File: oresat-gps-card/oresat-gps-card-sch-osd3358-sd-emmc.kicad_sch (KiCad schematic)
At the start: 21 parts, among them J4 DM3BT-DSF-PEJS, U1 OSD3358-512M-BSM, U8 TCAN330, U9 EMMC+RESET+5.1-COMPATIBLE-BA

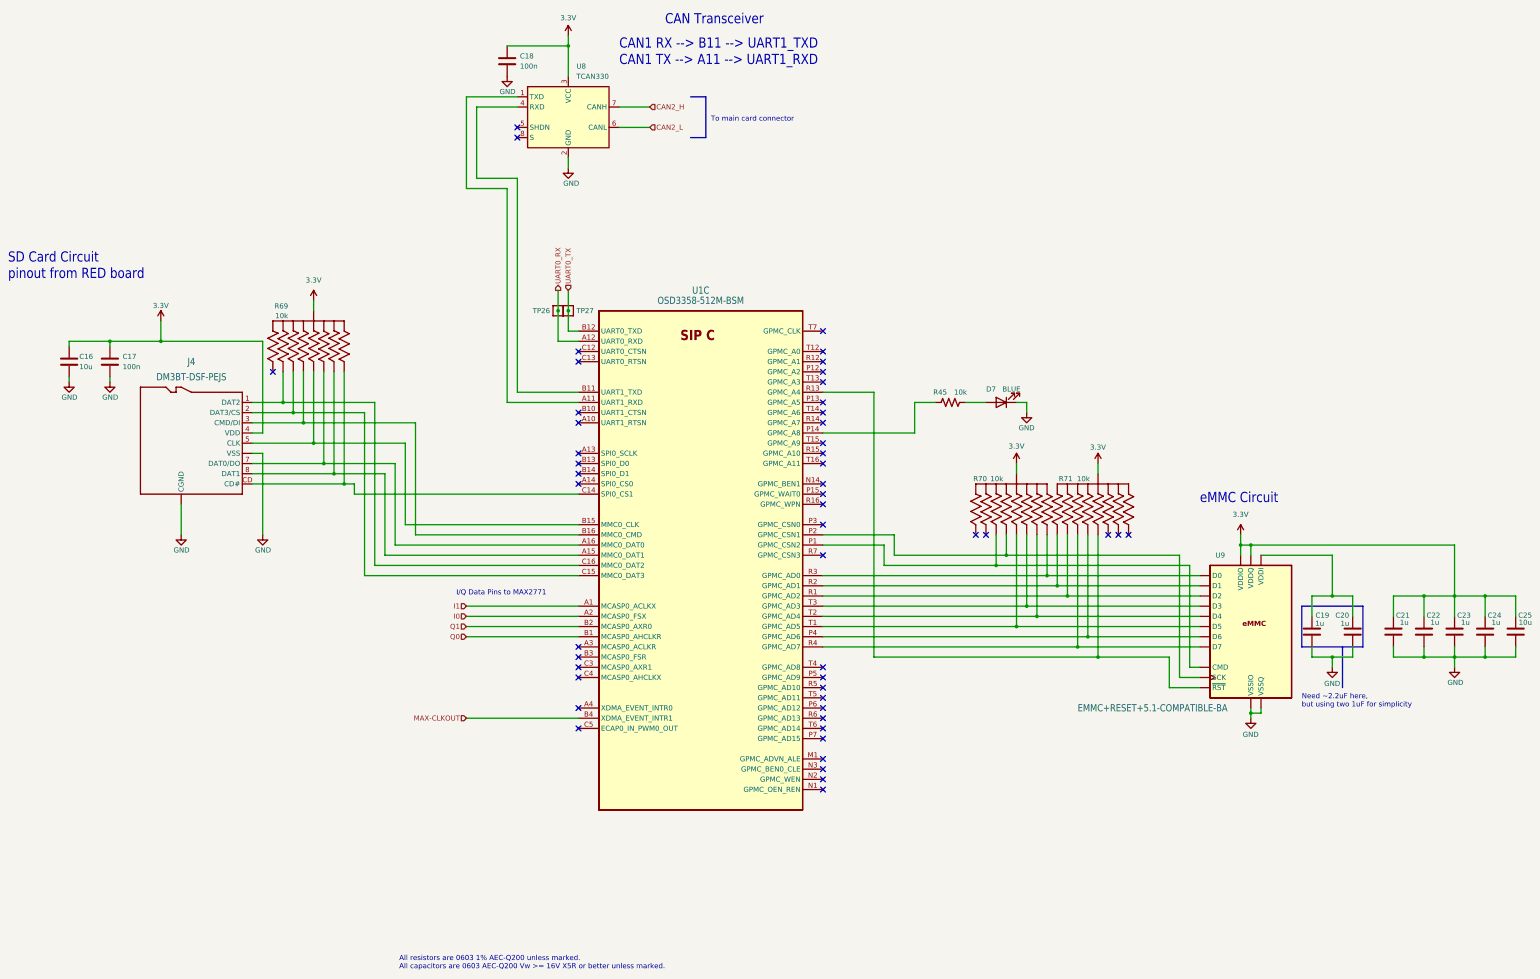
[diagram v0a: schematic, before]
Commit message: General cleanup of schematic and layout
Updated .gitignore, updates DRU file, moved RF lines to RF-50-MIN (max is just too big),
lots of cleanup on the root page to make it pretty, cleaned up some redudant labels,
updated SMPM connector and added rule zone, updated PCB outline to include NPTH drills
for SMPM connectors, began cleanup of OPD.
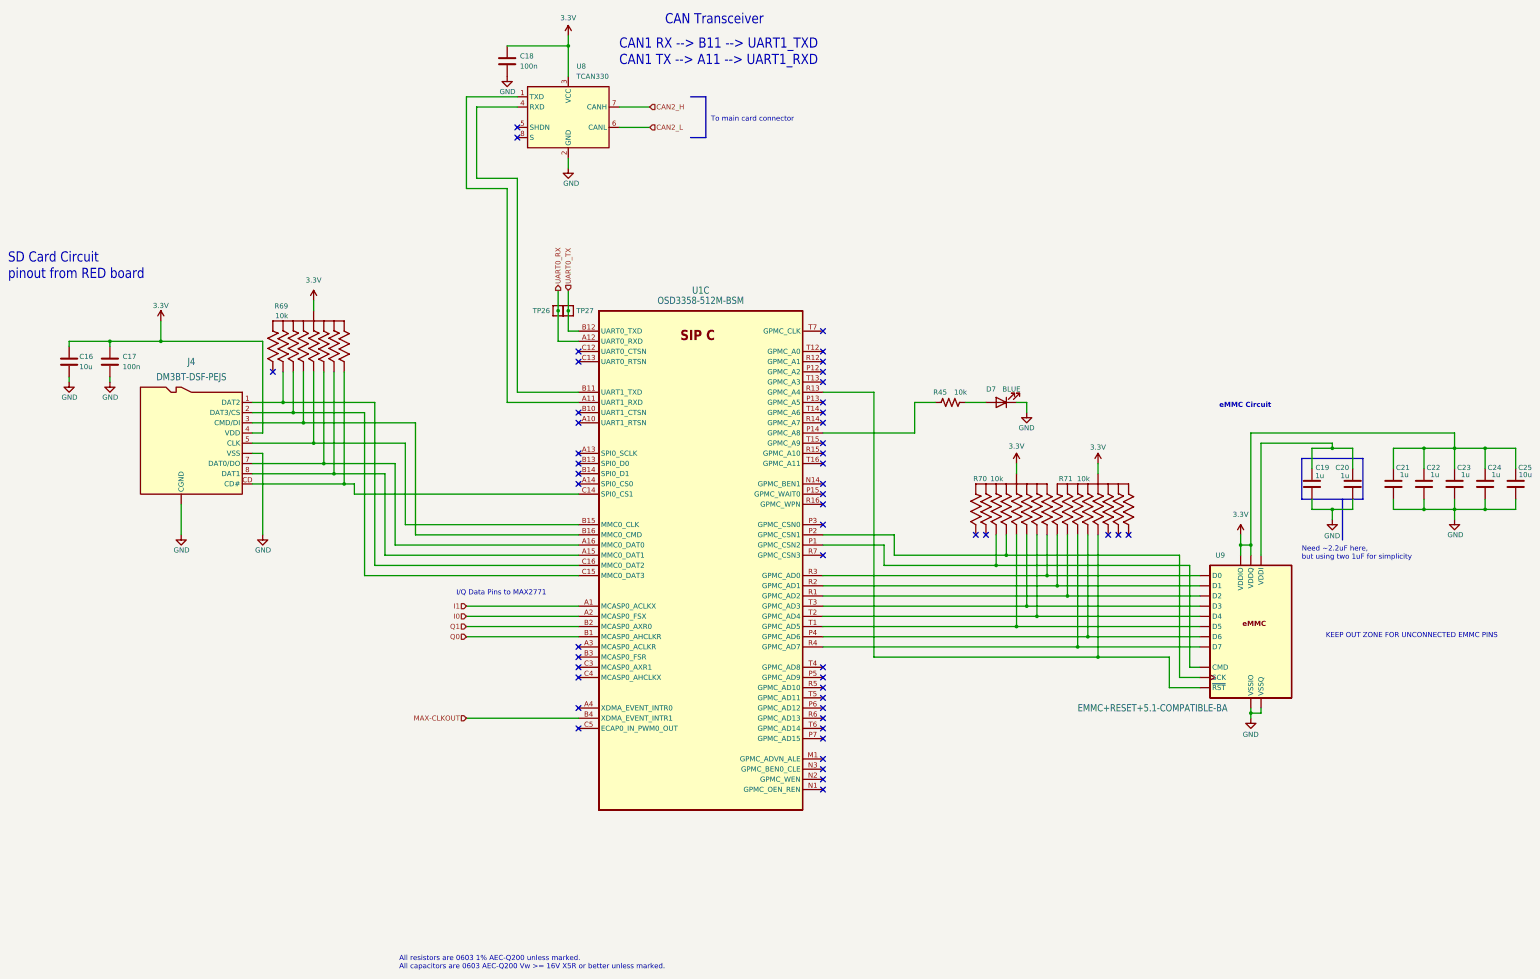
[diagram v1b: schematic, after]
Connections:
- net GND: no longer U9.A12 (NC), U9.A13 (NC)
- net at C19.1, C20.1, U9.C2 (VDDI): no longer U9.A2 (NC)
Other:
- note added: "KEEP OUT ZONE FOR UNCONNECTED EMMC PINS"
- moved on the sheet: C19, C20, C21, C22, C23, C24, C25
